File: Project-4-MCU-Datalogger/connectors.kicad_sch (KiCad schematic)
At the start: 4 parts, among them J1 Conn_01x04_Pin, J2 Conn_01x04_Pin, J3 Conn_01x09_Pin, J4 Conn_02x03_Odd_Even

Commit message: assign footprints, inc imported footprints
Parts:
- J1, J2: footprint (none) -> Connector_PinHeader_2.54mm:PinHeader_1x04_P2.54mm_Vertical
- J3: footprint (none) -> Connector_PinHeader_2.54mm:PinHeader_1x09_P2.54mm_Vertical
- J4: footprint (none) -> Connector_PinHeader_2.54mm:PinHeader_2x03_P2.54mm_Vertical
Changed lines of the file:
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@@
 			)
 		)
-		(property "Footprint" ""
+		(property "Footprint" "Connector_PinHeader_2.54mm:PinHeader_2x03_P2.54mm_Vertical"
 			(at 146.05 97.79 0)
 			(hide yes)
@@
 			)
 		)
-		(property "Footprint" ""
+		(property "Footprint" "Connector_PinHeader_2.54mm:PinHeader_1x09_P2.54mm_Vertical"
 			(at 120.65 104.14 0)
 			(hide yes)
@@
 			)
 		)
-		(property "Footprint" ""
+		(property "Footprint" "Connector_PinHeader_2.54mm:PinHeader_1x04_P2.54mm_Vertical"
 			(at 119.38 74.93 0)
 			(hide yes)
@@
 			)
 		)
-		(property "Footprint" ""
+		(property "Footprint" "Connector_PinHeader_2.54mm:PinHeader_1x04_P2.54mm_Vertical"
 			(at 142.24 74.93 0)
 			(hide yes)

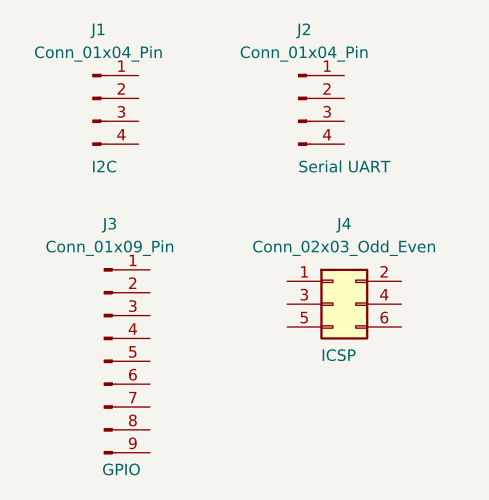
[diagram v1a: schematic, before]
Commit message: wire hierarchical child sheet, add hierarchical labels, connect sheets, run ERC
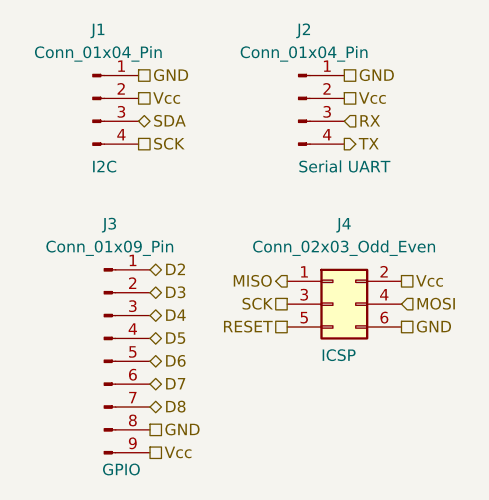
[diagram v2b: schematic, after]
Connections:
- net MISO: now reaches J4.1 (Pin_1)
- net Vcc: now reaches J4.2 (Pin_2)
- net Vcc: now also J1.2 (Pin_2), J2.2 (Pin_2), J3.9 (Pin_9)
- net SCK: now reaches J4.3 (Pin_3)
- net SCK: now also J1.4 (Pin_4)
- net MOSI: now reaches J4.4 (Pin_4)
- net RESET: now reaches J4.5 (Pin_5)
- net GND: now reaches J4.6 (Pin_6)
- net GND: now also J1.1 (Pin_1), J2.1 (Pin_1), J3.8 (Pin_8)
- net D2: now reaches J3.1 (Pin_1)
- net D3: now reaches J3.2 (Pin_2)
- net D4: now reaches J3.3 (Pin_3)
- net D5: now reaches J3.4 (Pin_4)
- net D6: now reaches J3.5 (Pin_5)
- net D7: now reaches J3.6 (Pin_6)
- net D8: now reaches J3.7 (Pin_7)
- net SDA: now reaches J1.3 (Pin_3)
- net RX: now reaches J2.3 (Pin_3)
- net TX: now reaches J2.4 (Pin_4)
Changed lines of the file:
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@@
 	(generator_version "10.0")
 	(paper "A4")
+	(hierarchical_label "D5"
+		(shape bidirectional)
+		(at 125.73 101.6 0)
+		(effects
+			(font
+				(size 1.27 1.27)
+			)
+			(justify left)
+		)
+	)
+	(hierarchical_label "RESET"
+		(shape passive)
+		(at 140.97 100.33 180)
+		(effects
+			(font
+				(size 1.27 1.27)
+			)
+			(justify right)
+		)
+	)
+	(hierarchical_label "GND"
+		(shape passive)
+		(at 147.32 72.39 0)
+		(effects
+			(font
+				(size 1.27 1.27)
+			)
+			(justify left)
+		)
+	)
+	(hierarchical_label "Vcc"
+		(shape passive)
+		(at 153.67 95.25 0)
+		(effects
+			(font
+				(size 1.27 1.27)
+			)
+			(justify left)
+		)
+	)
+	(hierarchical_label "D8"
+		(shape bidirectional)
+		(at 125.73 109.22 0)
+		(effects
+			(font
+				(size 1.27 1.27)
+			)
+			(justify left)
+		)
+	)
+	(hierarchical_label "SDA"
+		(shape bidirectional)
+		(at 124.46 77.47 0)
+		(effects
+			(font
+				(size 1.27 1.27)
+			)
+			(justify left)
+		)
+	)
+	(hierarchical_label "TX"
+		(shape output)
+		(at 147.32 80.01 0)
+		(effects
+			(font
+				(size 1.27 1.27)
+			)
+			(justify left)
+		)
+	)
+	(hierarchical_label "SCK"
+		(shape passive)
+		(at 124.46 80.01 0)
+		(effects
+			(font
+				(size 1.27 1.27)
+			)
+			(justify left)
+		)
+	)
+	(hierarchical_label "D2"
+		(shape bidirectional)
+		(at 125.73 93.98 0)
+		(effects
+			(font
+				(size 1.27 1.27)
+			)
+			(justify left)
+		)
+	)
+	(hierarchical_label "D4"
+		(shape bidirectional)
+		(at 125.73 99.06 0)
+		(effects
+			(font
+				(size 1.27 1.27)
+			)
+			(justify left)
+		)
+	)
+	(hierarchical_label "GND"
+		(shape passive)
+		(at 125.73 111.76 0)
+		(effects
+			(font
+				(size 1.27 1.27)
+			)
+			(justify left)
+		)
+	)
+	(hierarchical_label "D7"
+		(shape bidirectional)
+		(at 125.73 106.68 0)
+		(effects
+			(font
+				(size 1.27 1.27)
+			)
+			(justify left)
+		)
+	)
+	(hierarchical_label "GND"
+		(shape passive)
+		(at 124.46 72.39 0)
+		(effects
+			(font
+				(size 1.27 1.27)
+			)
+			(justify left)
+		)
+	)
+	(hierarchical_label "Vcc"
+		(shape passive)
+		(at 124.46 74.93 0)
+		(effects
+			(font
+				(size 1.27 1.27)
+			)
+			(justify left)
+		)
+	)
+	(hierarchical_label "MISO"
+		(shape output)
+		(at 140.97 95.25 180)
+		(effects
+			(font
+				(size 1.27 1.27)
+			)
+			(justify right)
+		)
+	)
+	(hierarchical_label "GND"
+		(shape passive)
+		(at 153.67 100.33 0)
+		(effects
+			(font
+				(size 1.27 1.27)
+			)
+			(justify left)
+		)
+	)
+	(hierarchical_label "D3"
+		(shape bidirectional)
+		(at 125.73 96.52 0)
+		(effects
+			(font
+				(size 1.27 1.27)
+			)
+			(justify left)
+		)
+	)
+	(hierarchical_label "SCK"
+		(shape passive)
+		(at 140.97 97.79 180)
+		(effects
+			(font
+				(size 1.27 1.27)
+			)
+			(justify right)
+		)
+	)
+	(hierarchical_label "Vcc"
+		(shape passive)
+		(at 125.73 114.3 0)
+		(effects
+			(font
+				(size 1.27 1.27)
+			)
+			(justify left)
+		)
+	)
+	(hierarchical_label "RX"
+		(shape input)
+		(at 147.32 77.47 0)
+		(effects
+			(font
+				(size 1.27 1.27)
+			)
+			(justify left)
+		)
+	)
+	(hierarchical_label "MOSI"
+		(shape input)
+		(at 153.67 97.79 0)
+		(effects
+			(font
+				(size 1.27 1.27)
+			)
+			(justify left)
+		)
+	)
+	(hierarchical_label "Vcc"
+		(shape passive)
+		(at 147.32 74.93 0)
+		(effects
+			(font
+				(size 1.27 1.27)
+			)
+			(justify left)
+		)
+	)
+	(hierarchical_label "D6"
+		(shape bidirectional)
+		(at 125.73 104.14 0)
+		(effects
+			(font
+				(size 1.27 1.27)
+			)
+			(justify left)
+		)
+	)
 	(symbol
 		(lib_id "Connector_Generic:Conn_02x03_Odd_Even")

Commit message: bugfix I2C's clock signal net label (rename from SCK to SCL)
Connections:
- net SCK: no longer J1.4 (Pin_4)
- new net SCL: J1.4 (Pin_4)
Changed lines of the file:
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@@
 		)
 	)
-	(hierarchical_label "SCK"
+	(hierarchical_label "SCL"
 		(shape passive)
 		(at 124.46 80.01 0)
